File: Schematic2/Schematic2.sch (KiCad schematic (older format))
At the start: 41 parts, among them U1 Kailhlowprofile, U10 Kailhlowprofile, U11 Kailhlowprofile, U12 Kailhlowprofile, U13 Kailhlowprofile, U14 Kailhlowprofile, U15 Kailhlowprofile, U16 Kailhlowprofile, U17 Kailhlowprofile, U18 Kailhlowprofile, U19 Kailhlowprofile, U2 Kailhlowprofile, U20 Kailhlowprofile, U3 Kailhlowprofile, U4 Kailhlowprofile, U5 Kailhlowprofile, U6 Kailhlowprofile, U7 Kailhlowprofile, U8 Kailhlowprofile, U9 Kailhlowprofile

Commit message: Schematic3
19/03/2019 23:59
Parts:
- U1, U10, U11, U12, U13, U14, U15, U16, U17, U18, U19, U2, U20, U3, U4, U5, U6, U7, U8, U9: footprint keyswitches:Kailh_socket_optional_reversible -> Keebio-Parts:Kailh-PG1350-1u-No-Clickhole
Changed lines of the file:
@@
 EESchema Schematic File Version 4
+LIBS:Schematic2-cache
 EELAYER 29 0
 EELAYER END
@@
 F 0 "U2" H 1125 727 50  0000 C CNN
 F 1 "Kailhlowprofile" H 1125 636 50  0000 C CNN
-F 2 "keyswitches:Kailh_socket_optional_reversible" H 1165 1220 50  0001 C CNN
+F 2 "Keebio-Parts:Kailh-PG1350-1u-No-Clickhole" H 1165 1220 50  0001 C CNN
 F 3 "" H 1165 1220 50  0001 C CNN
 	1    1500 1150
@@
 F 0 "U7" H 3258 1208 50  0000 L CNN
 F 1 "Kailhlowprofile" H 3258 1117 50  0000 L CNN
-F 2 "keyswitches:Kailh_socket_optional_reversible" H 2765 1220 50  0001 C CNN
+F 2 "Keebio-Parts:Kailh-PG1350-1u-No-Clickhole" H 2765 1220 50  0001 C CNN
 F 3 "" H 2765 1220 50  0001 C CNN
 	1    3100 1150
@@
 F 0 "U12" H 5008 1208 50  0000 L CNN
 F 1 "Kailhlowprofile" H 5008 1117 50  0000 L CNN
-F 2 "keyswitches:Kailh_socket_optional_reversible" H 4515 1220 50  0001 C CNN
+F 2 "Keebio-Parts:Kailh-PG1350-1u-No-Clickhole" H 4515 1220 50  0001 C CNN
 F 3 "" H 4515 1220 50  0001 C CNN
 	1    4850 1150
@@
 F 0 "U17" H 6808 1258 50  0000 L CNN
 F 1 "Kailhlowprofile" H 6808 1167 50  0000 L CNN
-F 2 "keyswitches:Kailh_socket_optional_reversible" H 6315 1270 50  0001 C CNN
+F 2 "Keebio-Parts:Kailh-PG1350-1u-No-Clickhole" H 6315 1270 50  0001 C CNN
 F 3 "" H 6315 1270 50  0001 C CNN
 	1    6650 1200
@@
 F 0 "U1" H 1125 2077 50  0000 C CNN
 F 1 "Kailhlowprofile" H 1125 1986 50  0000 C CNN
-F 2 "keyswitches:Kailh_socket_optional_reversible" H 1165 2570 50  0001 C CNN
+F 2 "Keebio-Parts:Kailh-PG1350-1u-No-Clickhole" H 1165 2570 50  0001 C CNN
 F 3 "" H 1165 2570 50  0001 C CNN
 	1    1500 2500
@@
 F 0 "U6" H 3258 2558 50  0000 L CNN
 F 1 "Kailhlowprofile" H 3258 2467 50  0000 L CNN
-F 2 "keyswitches:Kailh_socket_optional_reversible" H 2765 2570 50  0001 C CNN
+F 2 "Keebio-Parts:Kailh-PG1350-1u-No-Clickhole" H 2765 2570 50  0001 C CNN
 F 3 "" H 2765 2570 50  0001 C CNN
 	1    3100 2500
@@
 F 0 "U11" H 5008 2558 50  0000 L CNN
 F 1 "Kailhlowprofile" H 5008 2467 50  0000 L CNN
-F 2 "keyswitches:Kailh_socket_optional_reversible" H 4515 2570 50  0001 C CNN
+F 2 "Keebio-Parts:Kailh-PG1350-1u-No-Clickhole" H 4515 2570 50  0001 C CNN
 F 3 "" H 4515 2570 50  0001 C CNN
 	1    4850 2500
@@
 F 0 "U16" H 6808 2608 50  0000 L CNN
 F 1 "Kailhlowprofile" H 6808 2517 50  0000 L CNN
-F 2 "keyswitches:Kailh_socket_optional_reversible" H 6315 2620 50  0001 C CNN
+F 2 "Keebio-Parts:Kailh-PG1350-1u-No-Clickhole" H 6315 2620 50  0001 C CNN
 F 3 "" H 6315 2620 50  0001 C CNN
 	1    6650 2550
@@
 F 0 "U3" H 1125 3427 50  0000 C CNN
 F 1 "Kailhlowprofile" H 1125 3336 50  0000 C CNN
-F 2 "keyswitches:Kailh_socket_optional_reversible" H 1165 3920 50  0001 C CNN
+F 2 "Keebio-Parts:Kailh-PG1350-1u-No-Clickhole" H 1165 3920 50  0001 C CNN
 F 3 "" H 1165 3920 50  0001 C CNN
 	1    1500 3850
@@
 F 0 "U8" H 3258 3908 50  0000 L CNN
 F 1 "Kailhlowprofile" H 3258 3817 50  0000 L CNN
-F 2 "keyswitches:Kailh_socket_optional_reversible" H 2765 3920 50  0001 C CNN
+F 2 "Keebio-Parts:Kailh-PG1350-1u-No-Clickhole" H 2765 3920 50  0001 C CNN
 F 3 "" H 2765 3920 50  0001 C CNN
 	1    3100 3850
@@
 F 0 "U13" H 5008 3908 50  0000 L CNN
 F 1 "Kailhlowprofile" H 5008 3817 50  0000 L CNN
-F 2 "keyswitches:Kailh_socket_optional_reversible" H 4515 3920 50  0001 C CNN
+F 2 "Keebio-Parts:Kailh-PG1350-1u-No-Clickhole" H 4515 3920 50  0001 C CNN
 F 3 "" H 4515 3920 50  0001 C CNN
 	1    4850 3850
@@
 F 0 "U18" H 6808 3958 50  0000 L CNN
 F 1 "Kailhlowprofile" H 6808 3867 50  0000 L CNN
-F 2 "keyswitches:Kailh_socket_optional_reversible" H 6315 3970 50  0001 C CNN
+F 2 "Keebio-Parts:Kailh-PG1350-1u-No-Clickhole" H 6315 3970 50  0001 C CNN
 F 3 "" H 6315 3970 50  0001 C CNN
 	1    6650 3900
@@
 F 0 "U4" H 1125 4777 50  0000 C CNN
 F 1 "Kailhlowprofile" H 1125 4686 50  0000 C CNN
-F 2 "keyswitches:Kailh_socket_optional_reversible" H 1165 5270 50  0001 C CNN
+F 2 "Keebio-Parts:Kailh-PG1350-1u-No-Clickhole" H 1165 5270 50  0001 C CNN
 F 3 "" H 1165 5270 50  0001 C CNN
 	1    1500 5200
@@
 F 0 "U9" H 3258 5258 50  0000 L CNN
 F 1 "Kailhlowprofile" H 3258 5167 50  0000 L CNN
-F 2 "keyswitches:Kailh_socket_optional_reversible" H 2765 5270 50  0001 C CNN
+F 2 "Keebio-Parts:Kailh-PG1350-1u-No-Clickhole" H 2765 5270 50  0001 C CNN
 F 3 "" H 2765 5270 50  0001 C CNN
 	1    3100 5200
@@
 F 0 "U14" H 5008 5258 50  0000 L CNN
 F 1 "Kailhlowprofile" H 5008 5167 50  0000 L CNN
-F 2 "keyswitches:Kailh_socket_optional_reversible" H 4515 5270 50  0001 C CNN
+F 2 "Keebio-Parts:Kailh-PG1350-1u-No-Clickhole" H 4515 5270 50  0001 C CNN
 F 3 "" H 4515 5270 50  0001 C CNN
 	1    4850 5200
@@
 F 0 "U19" H 6808 5308 50  0000 L CNN
 F 1 "Kailhlowprofile" H 6808 5217 50  0000 L CNN
-F 2 "keyswitches:Kailh_socket_optional_reversible" H 6315 5320 50  0001 C CNN
+F 2 "Keebio-Parts:Kailh-PG1350-1u-No-Clickhole" H 6315 5320 50  0001 C CNN
 F 3 "" H 6315 5320 50  0001 C CNN
 	1    6650 5250
@@
 F 0 "U5" H 1125 6077 50  0000 C CNN
 F 1 "Kailhlowprofile" H 1125 5986 50  0000 C CNN
-F 2 "keyswitches:Kailh_socket_optional_reversible" H 1165 6570 50  0001 C CNN
+F 2 "Keebio-Parts:Kailh-PG1350-1u-No-Clickhole" H 1165 6570 50  0001 C CNN
 F 3 "" H 1165 6570 50  0001 C CNN
 	1    1500 6500
@@
 F 0 "U10" H 3258 6558 50  0000 L CNN
 F 1 "Kailhlowprofile" H 3258 6467 50  0000 L CNN
-F 2 "keyswitches:Kailh_socket_optional_reversible" H 2765 6570 50  0001 C CNN
+F 2 "Keebio-Parts:Kailh-PG1350-1u-No-Clickhole" H 2765 6570 50  0001 C CNN
 F 3 "" H 2765 6570 50  0001 C CNN
 	1    3100 6500
@@
 F 0 "U15" H 5008 6558 50  0000 L CNN
 F 1 "Kailhlowprofile" H 5008 6467 50  0000 L CNN
-F 2 "keyswitches:Kailh_socket_optional_reversible" H 4515 6570 50  0001 C CNN
+F 2 "Keebio-Parts:Kailh-PG1350-1u-No-Clickhole" H 4515 6570 50  0001 C CNN
 F 3 "" H 4515 6570 50  0001 C CNN
 	1    4850 6500
@@
 F 0 "U20" H 6808 6608 50  0000 L CNN
 F 1 "Kailhlowprofile" H 6808 6517 50  0000 L CNN
-F 2 "keyswitches:Kailh_socket_optional_reversible" H 6315 6620 50  0001 C CNN
+F 2 "Keebio-Parts:Kailh-PG1350-1u-No-Clickhole" H 6315 6620 50  0001 C CNN
 F 3 "" H 6315 6620 50  0001 C CNN
 	1    6650 6550

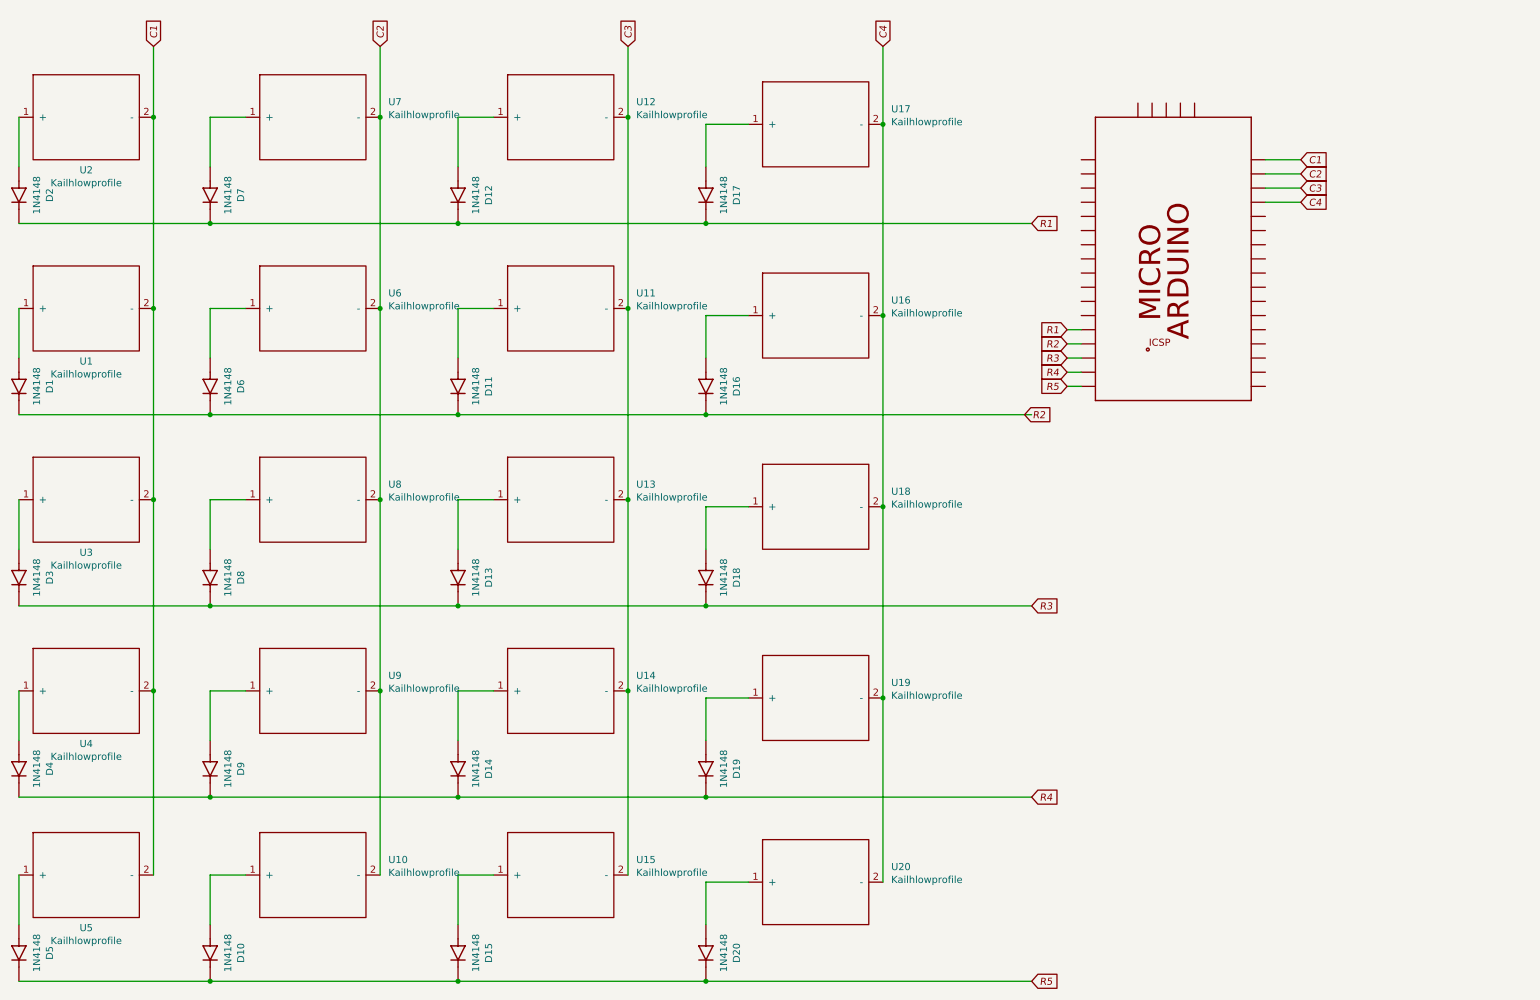
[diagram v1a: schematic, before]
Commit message: Finalized keyboard schem
Circuit finished
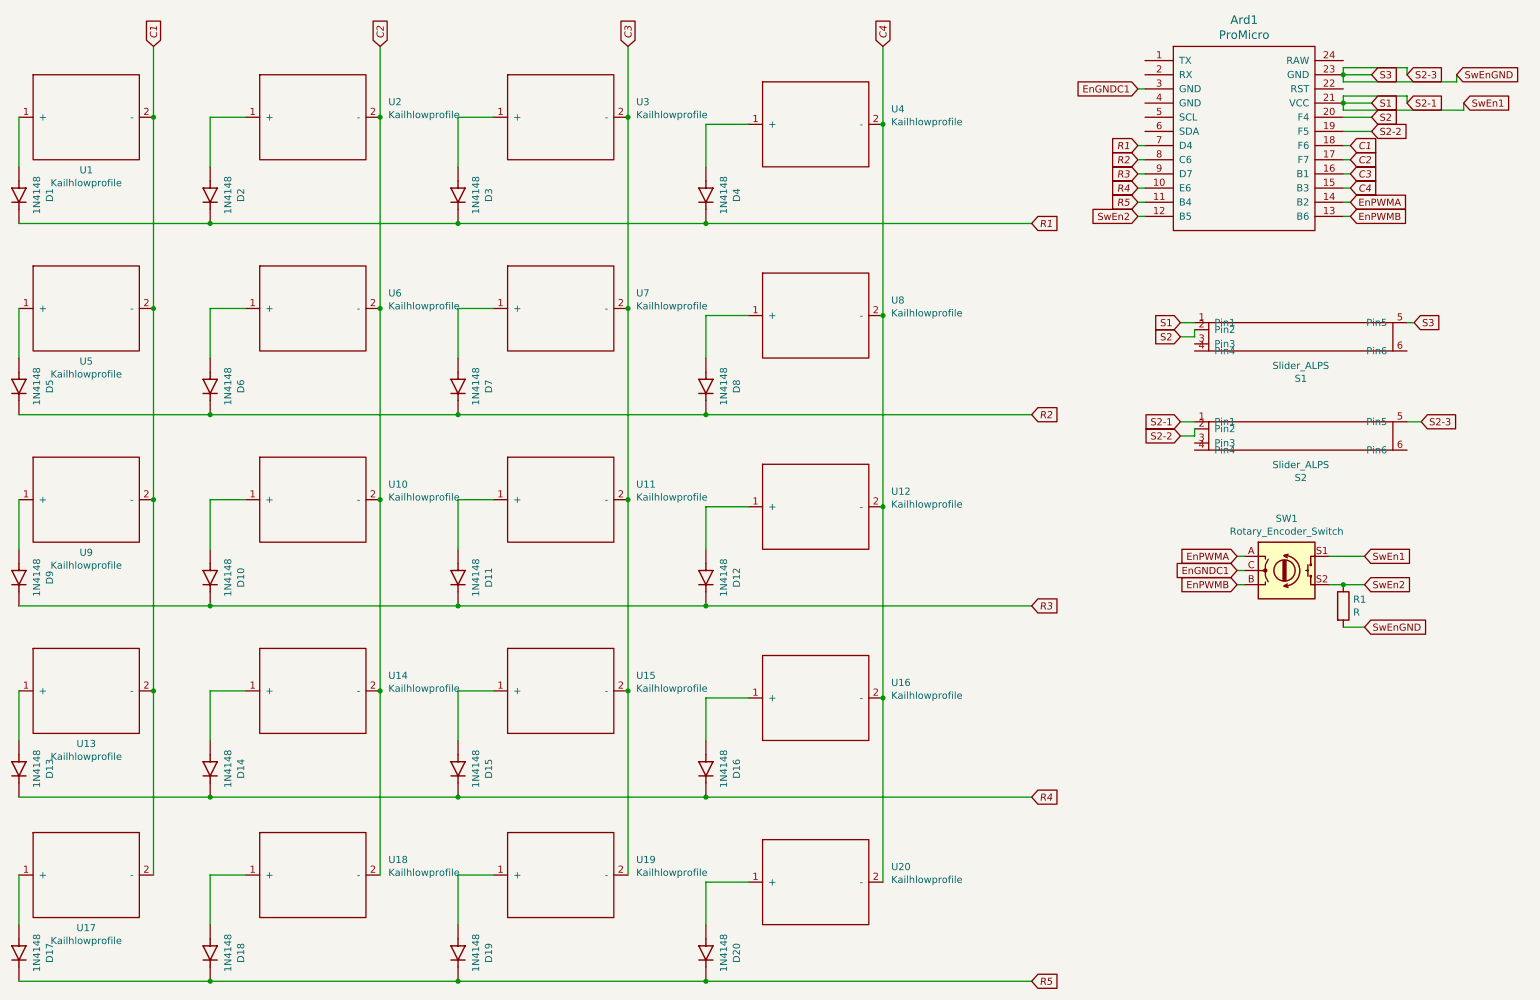
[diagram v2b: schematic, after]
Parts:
- removed PCB2: ARDUINO_MICRO, ARDUINO_MICRO:ARDUINO_MICRO, symbol ARDUINO_MICRO:ARDUINO_MICRO
- added Ard1: ProMicro, keebs:Pro_Micro, symbol promicro:ProMicro
- added R1: R, Resistor_THT:R_Axial_DIN0204_L3.6mm_D1.6mm_P2.54mm_Vertical, symbol Device:R
- added S1, S2: Slider_ALPS, alps_slider:ALPS-Slider, symbol Kailh:Slider_ALPS
- added SW1: Rotary_Encoder_Switch, Rotary_Encoder:RotaryEncoder_Alps_EC11E-Switch_Vertical_H20mm, symbol Device:Rotary_Encoder_Switch
- renumbered D2 to D1, D8 to D10, D13 to D11, D18 to D12, D4 to D13, D9 to D14, D14 to D15, D19 to D16, D5 to D17, D10 to D18, D15 to D19, D7 to D2, D12 to D3, D17 to D4, D1 to D5, D11 to D7, D16 to D8, D3 to D9, U2 to U1, U8 to U10, U13 to U11, U18 to U12, U4 to U13, U9 to U14, U14 to U15, U19 to U16, U5 to U17, U10 to U18, U15 to U19, U7 to U2, U12 to U3, U17 to U4, U1 to U5, U11 to U7, U16 to U8, U3 to U9
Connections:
- net C1: now also Ard1.18 (F6)
- net C2: now also Ard1.17 (F7)
- net C3: now also Ard1.16 (B1)
- net C4: now also Ard1.15 (B3)
- net R1: now also Ard1.7 (D4)
- net R2: now also Ard1.8 (C6)
- net R3: now also Ard1.9 (D7)
- net R4: now also Ard1.10 (E6)
- net R5: now also Ard1.11 (B4)
- new net EnGNDC1: Ard1.3 (GND), SW1.C
- new net EnPWMA: Ard1.14 (B2), SW1.A
- new net EnPWMB: Ard1.13 (B6), SW1.B
- new net S1: Ard1.21 (VCC), S1.1 (Pin1), S2.1 (Pin1), SW1.S1
- new net S2: Ard1.20 (F4), S1.2 (Pin2)
- new net S2-2: Ard1.19 (F5), S2.2 (Pin2)
- new net S2-3: Ard1.23 (GND), R1.2, S1.5 (Pin5), S2.5 (Pin5)
- new net SwEn2: Ard1.12 (B5), R1.1, SW1.S2

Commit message: New push 2019-03-21
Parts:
- removed D1, D10, D11, D12, D13, D14, D15, D16, D17, D18, D19, D2, D20, D3, D4, D5, D6, D7, D8, D9: 1N4148, 1N4148:DIOAD829W49L456D191, symbol 1N4148:1N4148
- added D1, D10, D11, D12, D13, D14, D15, D16, D17, D18, D19, D2, D20, D3, D4, D5, D6, D7, D8, D9: 1N4148WS, Diode_SMD:D_SOD-323, symbol Diode:1N4148WS
- added DI1, DI2, DI3, DI4, DI5, DI6, DI7: 1N4448WS, Diode_SMD:D_1206_3216Metric_Pad1.42x1.75mm_HandSolder, symbol Diode:1N4448WS
- U1, U10, U11, U12, U13, U14, U15, U16, U17, U18, U19, U2, U20, U3, U4, U5, U6, U7, U8, U9: footprint Keebio-Parts:Kailh-PG1350-1u-No-Clickhole -> Keebio-Parts:Kailh-PG1350-1u-No-Clickhole-No-LED
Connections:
- net S2-3 is gone; now on net EnGNDC1: Ard1.23 (GND), R1.2, S1.5 (Pin5), S2.5 (Pin5)
- net EnGNDC1: now also DI3.1 (K); no longer Ard1.3 (GND), SW1.C
- net EnPWMA: now also DI2.1 (K); no longer SW1.A
- net EnPWMB: now also DI4.1 (K); no longer SW1.B
- net R1: now also D1.1 (K), D2.1 (K), D3.1 (K), D4.1 (K)
- net R2: now also D5.1 (K), D6.1 (K), D7.1 (K), D8.1 (K)
- net R3: now also D10.1 (K), D11.1 (K), D12.1 (K), D9.1 (K)
- net R4: now also D13.1 (K), D14.1 (K), D15.1 (K), D16.1 (K)
- net R5: now also D17.1 (K), D18.1 (K), D19.1 (K), D20.1 (K)
- net S1: now also DI7.1 (K); no longer S1.1 (Pin1)
- net S2: now also DI6.1 (K); no longer S1.2 (Pin2)
- net S2-2: now also DI5.1 (K); no longer S2.2 (Pin2)
- net SwEn2: now also DI1.1 (K); no longer R1.1, SW1.S2
- net at U1.1 (+): now also D1.2 (A)
- net at U2.1 (+): now also D2.2 (A)
- net at U3.1 (+): now also D3.2 (A)
- net at U4.1 (+): now also D4.2 (A)
- net at U5.1 (+): now also D5.2 (A)
- net at U6.1 (+): now also D6.2 (A)
- net at U7.1 (+): now also D7.2 (A)
- net at U8.1 (+): now also D8.2 (A)
- net at U9.1 (+): now also D9.2 (A)
- net at U10.1 (+): now also D10.2 (A)
- net at U11.1 (+): now also D11.2 (A)
- net at U12.1 (+): now also D12.2 (A)
- net at U13.1 (+): now also D13.2 (A)
- net at U14.1 (+): now also D14.2 (A)
- net at U15.1 (+): now also D15.2 (A)
- net at U16.1 (+): now also D16.2 (A)
- net at U17.1 (+): now also D17.2 (A)
- net at U18.1 (+): now also D18.2 (A)
- net at U19.1 (+): now also D19.2 (A)
- net at U20.1 (+): now also D20.2 (A)
- new net: DI5.2 (A), S2.2 (Pin2)
- new net: DI7.2 (A), S1.1 (Pin1)
- new net: DI6.2 (A), S1.2 (Pin2)
- new net: DI2.2 (A), SW1.A
- new net: DI4.2 (A), SW1.B
- new net: DI3.2 (A), SW1.C
- new net: DI1.2 (A), R1.1, SW1.S2

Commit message: The final countdown
The diamond deluxe of FINAL
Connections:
- net EnGNDC1: now also DI3.2 (A), SW1.C
- net S1: now also DI7.2 (A), S1.1 (Pin1)
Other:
- moved on the sheet: DI7
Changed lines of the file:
@@
 S3
-Wire Wire Line
-	8850 2650 8950 2650
 Wire Wire Line
 	8850 2750 8950 2750
@@
 Text GLabel 8550 2750 0    50   Input ~ 0
 S2
-Text GLabel 8550 2650 0    50   Input ~ 0
+Text GLabel 8300 2650 0    50   Input ~ 0
 S1
 Text GLabel 10200 1200 2    50   Input ~ 0
@@
 	10000 4500 10150 4500
 Wire Wire Line
-	10000 4800 10150 4800
+	10000 4800 10100 4800
 Text GLabel 10800 900  2    50   Input ~ 0
 SwEnGND
@@
 Wire Wire Line
 	10000 950  10000 900
-Text GLabel 10800 700  2    50   Input ~ 0
-EnGNDC1
 Text GLabel 8650 4350 0    50   Input ~ 0
 EnGNDC1
@@
 L Diode:1N4448WS DI7
 U 1 1 5CAA900B
-P 8700 2650
-F 0 "DI7" H 8700 2867 50  0000 C CNN
-F 1 "1N4448WS" H 8700 2776 50  0000 C CNN
-F 2 "Diode_SMD:D_1206_3216Metric_Pad1.42x1.75mm_HandSolder" H 8700 2475 50  0001 C CNN
-F 3 "https://www.vishay.com/docs/81387/1n4448ws.pdf" H 8700 2650 50  0001 C CNN
-	1    8700 2650
+P 8450 2650
+F 0 "DI7" H 8450 2867 50  0000 C CNN
+F 1 "1N4448WS" H 8450 2776 50  0000 C CNN
+F 2 "Diode_SMD:D_1206_3216Metric_Pad1.42x1.75mm_HandSolder" H 8450 2475 50  0001 C CNN
+F 3 "https://www.vishay.com/docs/81387/1n4448ws.pdf" H 8450 2650 50  0001 C CNN
+	1    8450 2650
 	1    0    0    -1
 $EndComp
@@
 	9250 4250 9250 4300
 Wire Wire Line
-	9100 4400 9300 4400
-Wire Wire Line
 	9100 4550 9250 4550
 Wire Wire Line
@@
 Wire Wire Line
 	10750 950  10000 950
+Text GLabel 10800 700  2    50   Input ~ 0
+EnGNDC1
+Wire Wire Line
+	10100 4850 10100 4800
+Connection ~ 10100 4800
+Wire Wire Line
+	10100 4800 10150 4800
+Wire Wire Line
+	10100 4850 9200 4850
+Wire Wire Line
+	9200 4850 9200 4400
+Wire Wire Line
+	9100 4400 9200 4400
+Wire Wire Line
+	9200 4400 9300 4400
+Connection ~ 9200 4400
+Wire Wire Line
+	10450 3350 10450 3250
+Wire Wire Line
+	10450 3250 9200 3250
+Wire Wire Line
+	9200 3250 9200 4400
+Connection ~ 10450 3350
+Wire Wire Line
+	8600 2650 8700 2650
+Wire Wire Line
+	10150 4300 10150 2400
+Wire Wire Line
+	10150 2400 8800 2400
+Wire Wire Line
+	8800 2400 8800 2650
+Connection ~ 8800 2650
+Wire Wire Line
+	8800 2650 8950 2650
+Wire Wire Line
+	8950 3350 8950 2900
+Wire Wire Line
+	8950 2900 8700 2900
+Wire Wire Line
+	8700 2900 8700 2650
+Connection ~ 8950 3350
+Connection ~ 8700 2650
+Wire Wire Line
+	8700 2650 8800 2650
 $EndSCHEMATC
